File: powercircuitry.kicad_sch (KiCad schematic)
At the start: 160 parts, among them U1001 AM6231ASGGGAALW, U4001 TPS6521903RHBR, U4002 TLV62595DMQR

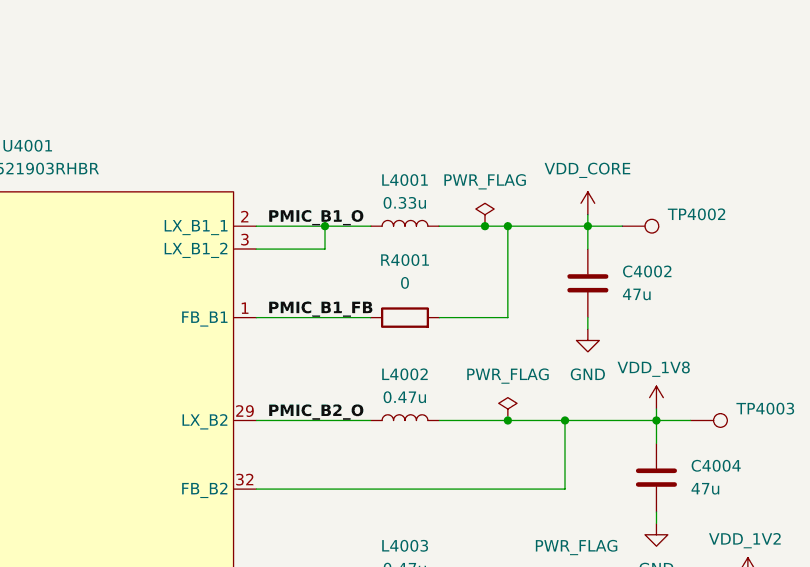
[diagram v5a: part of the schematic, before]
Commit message: Added almost all passive component footprints
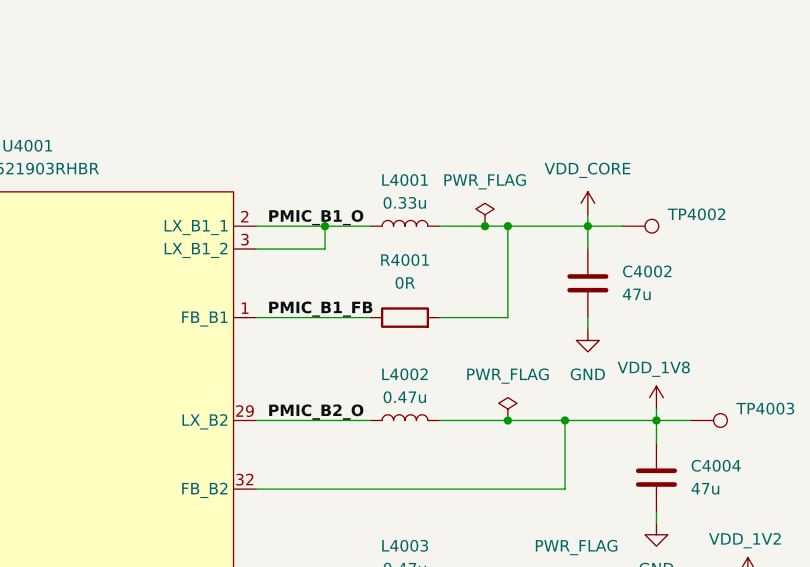
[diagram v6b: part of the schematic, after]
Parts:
- FB4001, FB4002, FB4003, FB4004, FB4005, FB4006, FB4007, FB4008, FB4009, FB4010, FB4011, R4002, R4003, R4004, R4005, R4006, R4007, R4008, R4009, R4010, R4011, R4012, R4013, R4014, R4015: footprint (none) -> Resistor_SMD:R_0402_1005Metric
- L4001, L4002, L4003, L4004: footprint (none) -> Inductor_SMD:L_1008_2520Metric
- R4001: value 0 -> 0R; footprint (none) -> Resistor_SMD:R_0402_1005Metric
- TP4001, TP4002, TP4003, TP4004, TP4005, TP4006, TP4007, TP4008: footprint (none) -> TestPoint:TestPoint_Pad_1.0x1.0mm
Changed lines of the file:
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@@
 			)
 		)
-		(property "Footprint" ""
+		(property "Footprint" "Resistor_SMD:R_0402_1005Metric"
 			(at 344.17 495.808 90)
 			(effects
@@
 			)
 		)
-		(property "Footprint" ""
+		(property "Footprint" "Resistor_SMD:R_0402_1005Metric"
 			(at 344.17 466.598 90)
 			(effects
@@
 			)
 		)
-		(property "Footprint" ""
+		(property "Footprint" "Resistor_SMD:R_0402_1005Metric"
 			(at 118.872 259.08 90)
 			(effects
@@
 			)
 		)
-		(property "Footprint" ""
+		(property "Footprint" "Resistor_SMD:R_0402_1005Metric"
 			(at 66.802 165.1 90)
 			(effects
@@
 			)
 		)
-		(property "Footprint" ""
+		(property "Footprint" "TestPoint:TestPoint_Pad_1.0x1.0mm"
 			(at 228.6 104.14 0)
 			(effects
@@
 			)
 		)
-		(property "Footprint" ""
+		(property "Footprint" "TestPoint:TestPoint_Pad_1.0x1.0mm"
 			(at 220.98 82.55 0)
 			(effects
@@
 			)
 		)
-		(property "Footprint" ""
+		(property "Footprint" "TestPoint:TestPoint_Pad_1.0x1.0mm"
 			(at 215.9 144.78 0)
 			(effects
@@
 			)
 		)
-		(property "Footprint" ""
+		(property "Footprint" "TestPoint:TestPoint_Pad_1.0x1.0mm"
 			(at 203.2 142.24 0)
 			(effects
@@
 			)
 		)
-		(property "Footprint" ""
+		(property "Footprint" "Resistor_SMD:R_0402_1005Metric"
 			(at 57.912 233.68 90)
 			(effects
@@
 			)
 		)
-		(property "Footprint" ""
+		(property "Footprint" "Resistor_SMD:R_0402_1005Metric"
 			(at 440.69 525.018 90)
 			(effects
@@
 			)
 		)
-		(property "Footprint" ""
+		(property "Footprint" "TestPoint:TestPoint_Pad_1.0x1.0mm"
 			(at 49.53 245.11 0)
 			(effects
@@
 			)
 		)
-		(property "Footprint" ""
+		(property "Footprint" "Resistor_SMD:R_0402_1005Metric"
 			(at 334.772 107.95 90)
 			(effects
@@
 			)
 		)
-		(property "Footprint" ""
+		(property "Footprint" "Resistor_SMD:R_0402_1005Metric"
 			(at 76.962 165.1 90)
 			(effects
@@
 			)
 		)
-		(property "Footprint" ""
+		(property "Footprint" "TestPoint:TestPoint_Pad_1.0x1.0mm"
 			(at 190.5 139.7 0)
 			(effects
@@
 			)
 		)
-		(property "Footprint" ""
+		(property "Footprint" "Resistor_SMD:R_0402_1005Metric"
 			(at 129.54 254.508 90)
 			(effects
@@
 			)
 		)
-		(property "Footprint" ""
+		(property "Footprint" "Resistor_SMD:R_0402_1005Metric"
 			(at 142.24 254.508 90)
 			(effects
@@
 			)
 		)
-		(property "Footprint" ""
+		(property "Footprint" "Resistor_SMD:R_0402_1005Metric"
 			(at 560.07 554.228 90)
 			(effects
@@
 			)
 		)
-		(property "Footprint" ""
+		(property "Footprint" "Inductor_SMD:L_1008_2520Metric"
 			(at 127 240.03 0)
 			(effects
@@
 			)
 		)
-		(property "Footprint" ""
+		(property "Footprint" "Resistor_SMD:R_0402_1005Metric"
 			(at 239.522 148.59 90)
 			(effects
@@
 			)
 		)
-		(property "Value" "0"
+		(property "Value" "0R"
 			(at 196.85 83.82 90)
 			(effects
@@
 			)
 		)
-		(property "Footprint" ""
+		(property "Footprint" "Resistor_SMD:R_0402_1005Metric"
 			(at 196.85 89.408 90)
 			(effects
@@
 			)
 		)
-		(property "Footprint" ""
+		(property "Footprint" "Resistor_SMD:R_0402_1005Metric"
 			(at 440.69 495.808 90)
 			(effects
@@
 			)
 		)
-		(property "Footprint" ""
+		(property "Footprint" "Resistor_SMD:R_0402_1005Metric"
 			(at 87.122 165.1 90)
 			(effects
@@
 			)
 		)
-		(property "Footprint" ""
+		(property "Footprint" "Resistor_SMD:R_0402_1005Metric"
 			(at 560.07 466.598 90)
 			(effects
@@
 			)
 		)
-		(property "Footprint" ""
+		(property "Footprint" "Resistor_SMD:R_0402_1005Metric"
 			(at 334.772 95.25 90)
 			(effects
@@
 			)
 		)
-		(property "Footprint" ""
+		(property "Footprint" "Inductor_SMD:L_1008_2520Metric"
 			(at 196.85 99.06 0)
 			(effects
@@
 			)
 		)
-		(property "Footprint" ""
+		(property "Footprint" "Resistor_SMD:R_0402_1005Metric"
 			(at 440.69 466.598 90)
 			(effects
@@
 			)
 		)
-		(property "Footprint" ""
+		(property "Footprint" "TestPoint:TestPoint_Pad_1.0x1.0mm"
 			(at 238.76 123.19 0)
 			(effects
@@
 			)
 		)
-		(property "Footprint" ""
+		(property "Footprint" "Resistor_SMD:R_0402_1005Metric"
 			(at 47.752 233.68 90)
 			(effects
@@
 			)
 		)
-		(property "Footprint" ""
+		(property "Footprint" "TestPoint:TestPoint_Pad_1.0x1.0mm"
 			(at 228.6 147.32 0)
 			(effects
@@
 			)
 		)
-		(property "Footprint" ""
+		(property "Footprint" "Resistor_SMD:R_0402_1005Metric"
 			(at 560.07 525.018 90)
 			(effects
@@
 			)
 		)
-		(property "Footprint" ""
+		(property "Footprint" "Resistor_SMD:R_0402_1005Metric"
 			(at 249.682 148.59 90)
 			(effects
@@
 			)
 		)
-		(property "Footprint" ""
+		(property "Footprint" "Resistor_SMD:R_0402_1005Metric"
 			(at 344.17 554.228 90)
 			(effects
@@
 			)
 		)
-		(property "Footprint" ""
+		(property "Footprint" "Resistor_SMD:R_0402_1005Metric"
 			(at 361.442 181.61 90)
 			(effects
@@
 			)
 		)
-		(property "Footprint" ""
+		(property "Footprint" "Resistor_SMD:R_0402_1005Metric"
 			(at 344.17 525.018 90)
 			(effects
@@
 			)
 		)
-		(property "Footprint" ""
+		(property "Footprint" "Inductor_SMD:L_1008_2520Metric"
 			(at 196.85 77.47 0)
 			(effects
@@
 			)
 		)
-		(property "Footprint" ""
+		(property "Footprint" "Resistor_SMD:R_0402_1005Metric"
 			(at 361.442 191.77 90)
 			(effects
@@
 			)
 		)
-		(property "Footprint" ""
+		(property "Footprint" "Inductor_SMD:L_1008_2520Metric"
 			(at 196.85 118.11 0)
 			(effects
@@
 			)
 		)
-		(property "Footprint" ""
+		(property "Footprint" "Resistor_SMD:R_0402_1005Metric"
 			(at 560.07 495.808 90)
 			(effects

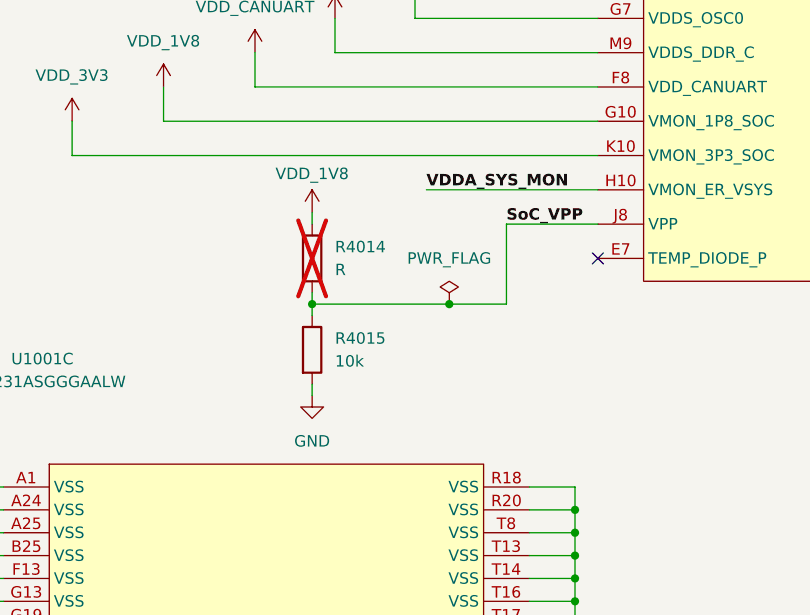
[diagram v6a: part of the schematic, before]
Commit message: Did fanout for SoC BGA power balls
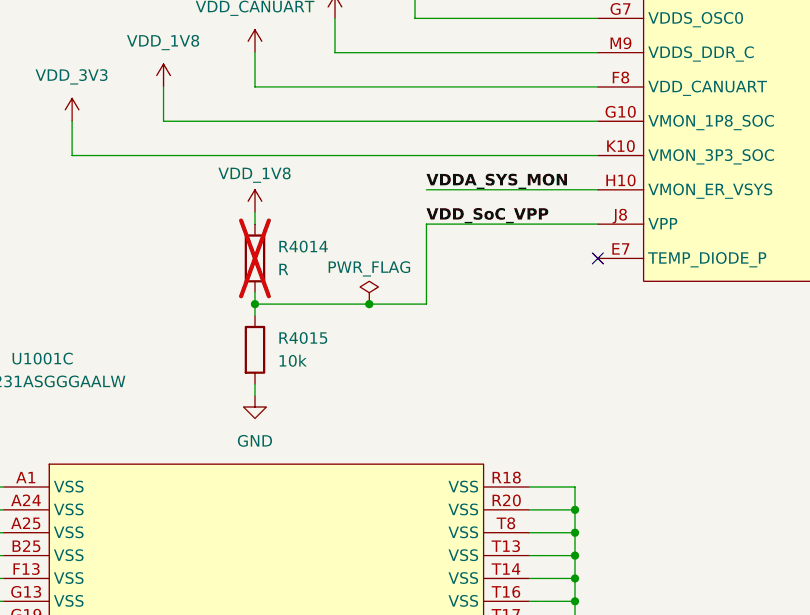
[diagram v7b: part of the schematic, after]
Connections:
- net SoC_VPP renamed VDD_SoC_VPP
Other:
- moved on the sheet: R4014, R4015
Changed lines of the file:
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@@
 	)
 	(junction
+		(at 356.87 186.69)
+		(diameter 0)
+		(color 0 0 0 0)
+	)
+	(junction
 		(at 495.3 336.55)
 		(diameter 0)
@@
 	)
 	(junction
+		(at 369.57 186.69)
+		(diameter 0)
+		(color 0 0 0 0)
+	)
+	(junction
 		(at 553.72 383.54)
 		(diameter 0)
@@
 	)
 	(junction
-		(at 363.22 186.69)
-		(diameter 0)
-		(color 0 0 0 0)
-	)
-	(junction
 		(at 431.8 336.55)
 		(diameter 0)
@@
 	)
 	(junction
-		(at 378.46 186.69)
-		(diameter 0)
-		(color 0 0 0 0)
-	)
-	(junction
 		(at 566.42 383.54)
 		(diameter 0)
@@
 	(wire
 		(pts
-			(xy 363.22 176.53) (xy 363.22 177.8)
+			(xy 356.87 176.53) (xy 356.87 177.8)
 		)
 		(stroke
@@
 	(wire
 		(pts
-			(xy 363.22 186.69) (xy 363.22 187.96)
+			(xy 356.87 186.69) (xy 356.87 187.96)
 		)
 		(stroke
@@
 	(wire
 		(pts
-			(xy 378.46 186.69) (xy 384.81 186.69)
-		)
-		(stroke
-			(width 0)
-			(type default)
-		)
-	)
-	(wire
-		(pts
 			(xy 234.95 128.27) (xy 234.95 129.54)
 		)
@@
 	(wire
 		(pts
+			(xy 356.87 186.69) (xy 369.57 186.69)
+		)
+		(stroke
+			(width 0)
+			(type default)
+		)
+	)
+	(wire
+		(pts
 			(xy 461.01 166.37) (xy 544.83 166.37)
 		)
@@
 	(wire
 		(pts
-			(xy 384.81 177.8) (xy 394.97 177.8)
+			(xy 375.92 177.8) (xy 394.97 177.8)
 		)
 		(stroke
@@
 	(wire
 		(pts
-			(xy 363.22 186.69) (xy 378.46 186.69)
-		)
-		(stroke
-			(width 0)
-			(type default)
-		)
-	)
-	(wire
-		(pts
 			(xy 74.93 139.7) (xy 88.9 139.7)
 		)
@@
 	(wire
 		(pts
-			(xy 384.81 186.69) (xy 384.81 177.8)
+			(xy 375.92 186.69) (xy 375.92 177.8)
 		)
 		(stroke
@@
 	(wire
 		(pts
-			(xy 363.22 185.42) (xy 363.22 186.69)
+			(xy 356.87 185.42) (xy 356.87 186.69)
 		)
 		(stroke
@@
 	(wire
 		(pts
-			(xy 363.22 195.58) (xy 363.22 196.85)
+			(xy 356.87 195.58) (xy 356.87 196.85)
 		)
 		(stroke
@@
 	(wire
 		(pts
+			(xy 369.57 186.69) (xy 375.92 186.69)
+		)
+		(stroke
+			(width 0)
+			(type default)
+		)
+	)
+	(wire
+		(pts
 			(xy 393.7 405.13) (xy 406.4 405.13)
 		)
@@
 		)
 	)
-	(label "SoC_VPP"
-		(at 384.81 177.8 0)
+	(label "VDD_SoC_VPP"
+		(at 375.92 177.8 0)
 		(effects
 			(font
@@
 	(symbol
 		(lib_id "power:PWR_FLAG")
-		(at 378.46 186.69 0)
+		(at 369.57 186.69 0)
 		(unit 1)
 		(exclude_from_sim no)
@@
 		(on_board yes)
 		(dnp no)
-		(fields_autoplaced yes)
 		(property "Reference" "#FLG04018"
-			(at 378.46 184.785 0)
+			(at 369.57 184.785 0)
 			(effects
 				(font
@@
 		)
 		(property "Value" "PWR_FLAG"
-			(at 378.46 181.61 0)
+			(at 369.57 182.626 0)
 			(effects
 				(font
@@
 		)
 		(property "Footprint" ""
-			(at 378.46 186.69 0)
+			(at 369.57 186.69 0)
 			(effects
 				(font
@@
 		)
 		(property "Datasheet" "~"
-			(at 378.46 186.69 0)
+			(at 369.57 186.69 0)
 			(effects
 				(font
@@
 		)
 		(property "Description" "Special symbol for telling ERC where power comes from"
-			(at 378.46 186.69 0)
+			(at 369.57 186.69 0)
 			(effects
 				(font
@@
 	(symbol
 		(lib_id "power:GND")
-		(at 363.22 196.85 0)
+		(at 356.87 196.85 0)
 		(unit 1)
 		(exclude_from_sim no)
@@
 		(fields_autoplaced yes)
 		(property "Reference" "#PWR04131"
-			(at 363.22 203.2 0)
+			(at 356.87 203.2 0)
 			(effects
 				(font
@@
 		)
 		(property "Value" "GND"
-			(at 363.22 201.93 0)
+			(at 356.87 201.93 0)
 			(effects
 				(font
@@
 		)
 		(property "Footprint" ""
-			(at 363.22 196.85 0)
+			(at 356.87 196.85 0)
 			(effects
 				(font
@@
 		)
 		(property "Datasheet" ""
-			(at 363.22 196.85 0)
+			(at 356.87 196.85 0)
 			(effects
 				(font
@@
 		)
 		(property "Description" "Power symbol creates a global label with name \"GND\" , ground"
-			(at 363.22 196.85 0)
+			(at 356.87 196.85 0)
 			(effects
 				(font
@@
 	(symbol
 		(lib_id "power:VDD")
-		(at 363.22 176.53 0)
+		(at 356.87 176.53 0)
 		(unit 1)
 		(exclude_from_sim no)
@@
 		(dnp no)
 		(property "Reference" "#PWR04063"
-			(at 363.22 180.34 0)
+			(at 356.87 180.34 0)
 			(effects
 				(font
@@
 		)
 		(property "Value" "VDD_1V8"
-			(at 363.22 172.212 0)
+			(at 356.87 172.212 0)
 			(effects
 				(font
@@
 		)
 		(property "Footprint" ""
-			(at 363.22 176.53 0)
+			(at 356.87 176.53 0)
 			(effects
 				(font
@@
 		)
 		(property "Datasheet" ""
-			(at 363.22 176.53 0)
+			(at 356.87 176.53 0)
 			(effects
 				(font
@@
 		)
 		(property "Description" "Power symbol creates a global label with name \"VDD\""
-			(at 363.22 176.53 0)
+			(at 356.87 176.53 0)
 			(effects
 				(font
@@
 	(symbol
 		(lib_id "Device:R")
-		(at 363.22 181.61 0)
+		(at 356.87 181.61 0)
 		(unit 1)
 		(exclude_from_sim no)
@@
 		(on_board yes)
 		(dnp yes)
-		(fields_autoplaced yes)
 		(property "Reference" "R4014"
-			(at 365.76 180.3399 0)
+			(at 359.41 180.3399 0)
 			(effects
 				(font
@@
 		)
 		(property "Value" "R"
-			(at 365.76 182.8799 0)
+			(at 359.41 182.8799 0)
 			(effects
 				(font
@@
 		)
 		(property "Footprint" "Resistor_SMD:R_0402_1005Metric"
-			(at 361.442 181.61 90)
+			(at 355.092 181.61 90)
 			(effects
 				(font
@@
 		)
 		(property "Datasheet" "~"
-			(at 363.22 181.61 0)
+			(at 356.87 181.61 0)
 			(effects
 				(font
@@
 		)
 		(property "Description" "Resistor"
-			(at 363.22 181.61 0)
+			(at 356.87 181.61 0)
 			(effects
 				(font
@@
 	(symbol
 		(lib_id "Device:R")
-		(at 363.22 191.77 0)
+		(at 356.87 191.77 0)
 		(unit 1)
 		(exclude_from_sim no)
@@
 		(fields_autoplaced yes)
 		(property "Reference" "R4015"
-			(at 365.76 190.4999 0)
+			(at 359.41 190.4999 0)
 			(effects
 				(font
@@
 		)
 		(property "Value" "10k"
-			(at 365.76 193.0399 0)
+			(at 359.41 193.0399 0)
 			(effects
 				(font
@@
 		)
 		(property "Footprint" "Resistor_SMD:R_0402_1005Metric"
-			(at 361.442 191.77 90)
+			(at 355.092 191.77 90)
 			(effects
 				(font
@@
 		)
 		(property "Datasheet" "~"
-			(at 363.22 191.77 0)
+			(at 356.87 191.77 0)
 			(effects
 				(font
@@
 		)
 		(property "Description" "Resistor"
-			(at 363.22 191.77 0)
+			(at 356.87 191.77 0)
 			(effects
 				(font

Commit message: Restarted SoC power decoupling based on manufacturer capabilities
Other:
- note added: "Power Circuitry"
- moved on the sheet: C4001, C4002, C4003, C4004, C4005, C4006, C4007, C4008, C4009, C4010, C4011, C4012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
